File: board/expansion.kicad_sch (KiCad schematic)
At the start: 2 parts, among them U13 ENGINE

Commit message: checkpoint
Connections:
- net A1: no longer names the net of U13.48 (I/O)
- net A10: no longer names the net of U13.39 (I/O)
- net A11: no longer names the net of U13.37 (I/O)
- net A12: no longer names the net of U13.29 (I/O)
- net A13: no longer names the net of U13.36 (I/O)
- net A14: no longer names the net of U13.75 (I/O)
- net A15: no longer names the net of U13.74 (I/O)
- net A16: no longer names the net of U13.56 (I/O)
- net A17: no longer names the net of U13.57 (I/O)
- net A18: no longer names the net of U13.31 (I/O)
- net A19: no longer names the net of U13.30 (I/O)
- net A2: no longer names the net of U13.49 (I/O)
- net A20: no longer names the net of U13.58 (I/O)
- net A21: no longer names the net of U13.28 (I/O)
- net A22: no longer names the net of U13.60 (I/O)
- net A23: no longer names the net of U13.61 (I/O)
- net A3: no longer names the net of U13.51 (I/O)
- net A4: no longer names the net of U13.54 (I/O)
- net A5: no longer names the net of U13.55 (I/O)
- net A6: no longer names the net of U13.52 (I/O)
- net A7: no longer names the net of U13.50 (I/O)
- net A8: no longer names the net of U13.45 (I/O/PD2)
- net A9: no longer names the net of U13.44 (I/O)
- net D0: no longer names the net of U13.18 (I/O)
- net D1: no longer names the net of U13.68 (I/O)
- net D10: no longer names the net of U13.67 (I/O)
- net D11: no longer names the net of U13.20 (I/O)
- net D12: no longer names the net of U13.65 (I/O)
- net D13: no longer names the net of U13.24 (I/O)
- net D14: no longer names the net of U13.63 (I/O)
- net D15: no longer names the net of U13.27 (I/O)
- net D2: no longer names the net of U13.17 (I/O)
- net D3: no longer names the net of U13.15 (I/O)
- net D4: no longer names the net of U13.12 (I/O/PD1)
- net D5: no longer names the net of U13.11 (I/O)
- net D6: no longer names the net of U13.73 (I/O)
- net D7: no longer names the net of U13.70 (I/O)
- net D8: no longer names the net of U13.16 (I/O)
- net D9: no longer names the net of U13.69 (I/O)
- net ENGINE_TCK: no longer names the net of U13.62 (I/O/TCK)
- net ENGINE_TDI: no longer names the net of U13.14 (I/O/TDI)
- net ENGINE_TDO: no longer names the net of U13.71 (I/O/TDO)
- net ENGINE_TMS: no longer names the net of U13.23 (I/O/TMS)
- net FC0: no longer names the net of U13.33 (I/O)
- net FC1: no longer names the net of U13.34 (I/O)
- net FC2: no longer names the net of U13.35 (I/O)
- net R/~{W}: no longer names the net of U13.25 (I/O)
- net SYSCLK: no longer names the net of U13.83 (INPUT/GCLK1)
- net ~{AS}: no longer names the net of U13.21 (I/O)
- net ~{BGACK}: no longer names the net of U13.77 (I/O)
- net ~{BG}: no longer names the net of U13.76 (I/O)
- net ~{BR}: no longer names the net of U13.79 (I/O)
- net ~{DTACK}: no longer names the net of U13.81 (I/O/GCLK3)
- net ~{ENGINE_DTACK}: no longer names the net of U13.4 (I/O)
- net ~{ENGINE_IRQ}: no longer names the net of U13.5 (I/O)
- net ~{ENGINE_SELECT}: no longer names the net of U13.84 (INPUT/OE1)
- net ~{LDS}: no longer names the net of U13.64 (I/O)
- net ~{RESET}: no longer names the net of U13.1 (INPUT/GCLR)
- net ~{UDS}: no longer names the net of U13.22 (I/O)
- no-connect marks 9 -> 1

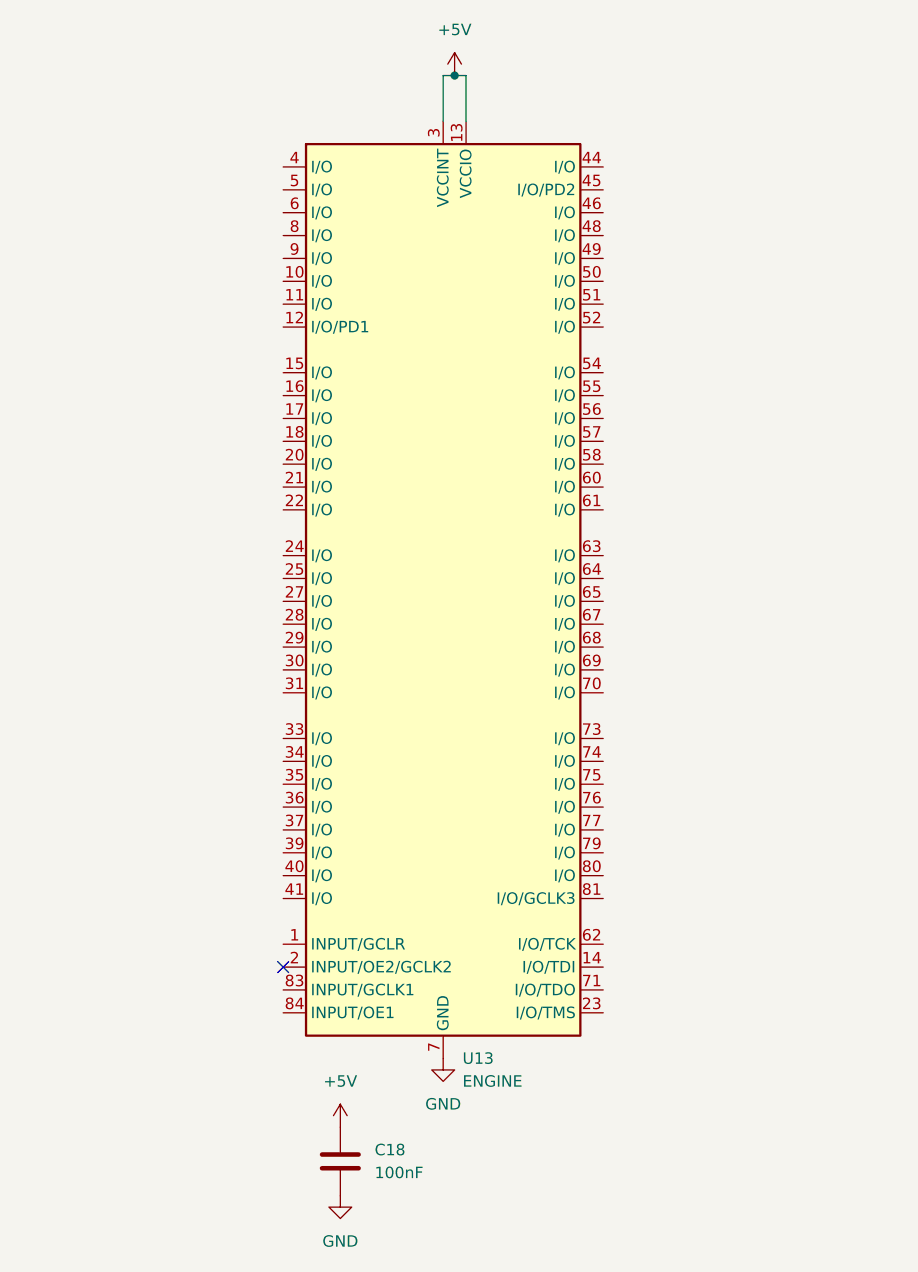
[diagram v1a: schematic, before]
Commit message: capture ENGINE in schematic; fix couple of shorts
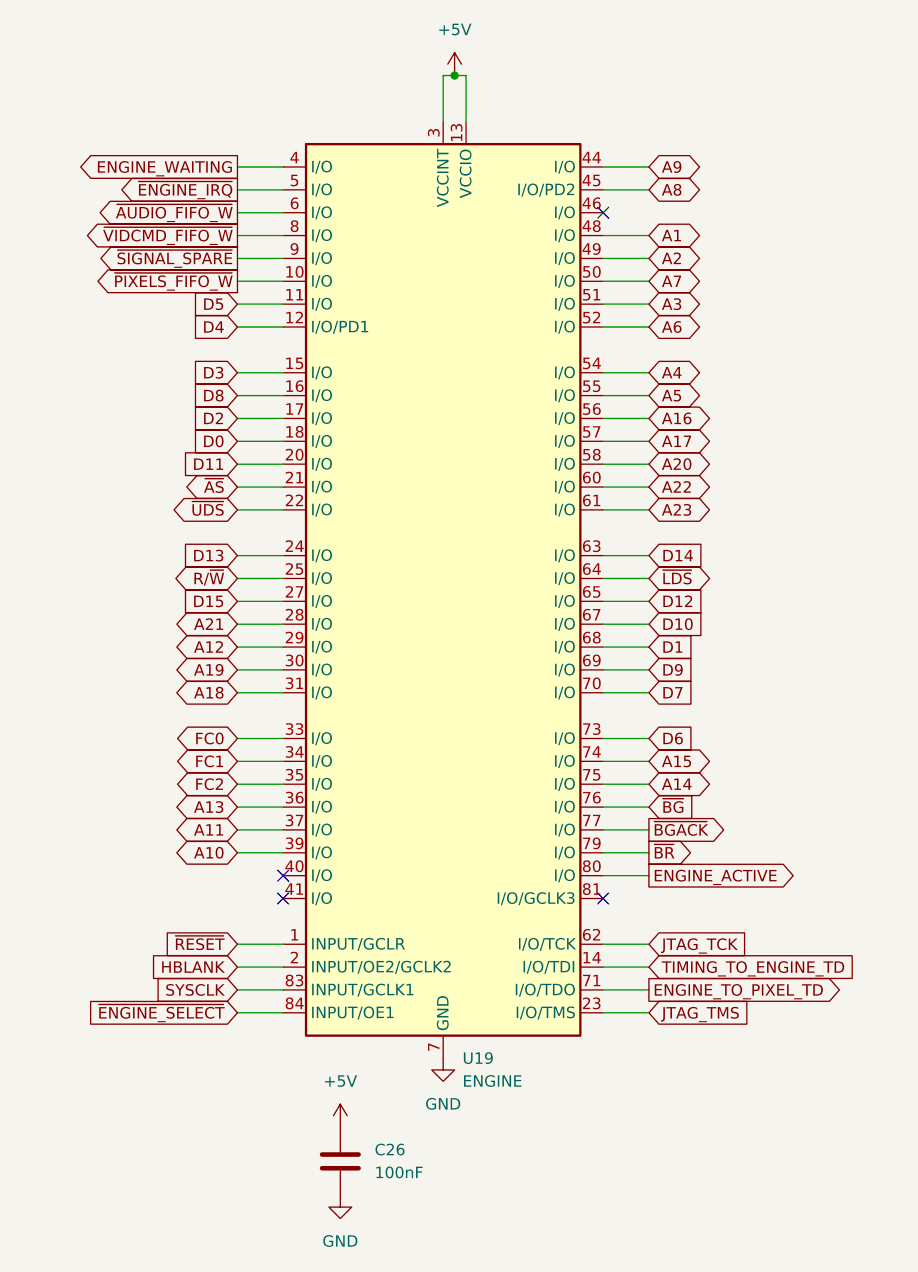
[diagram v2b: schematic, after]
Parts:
- renumbered C18 to C26, U13 to U19
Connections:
- net ~{RESET}: now reaches U19.1 (INPUT/GCLR)
- net ~{PIXELS_FIFO_W}: now reaches U19.10 (I/O)
- net D5: now reaches U19.11 (I/O)
- net D4: now reaches U19.12 (I/O/PD1)
- net TIMING_TO_ENGINE_TD: now reaches U19.14 (I/O/TDI)
- net D3: now reaches U19.15 (I/O)
- net D8: now reaches U19.16 (I/O)
- net D2: now reaches U19.17 (I/O)
- net D0: now reaches U19.18 (I/O)
- net HBLANK: now reaches U19.2 (INPUT/OE2/GCLK2)
- net D11: now reaches U19.20 (I/O)
- net ~{AS}: now reaches U19.21 (I/O)
- net ~{UDS}: now reaches U19.22 (I/O)
- net JTAG_TMS: now reaches U19.23 (I/O/TMS)
- net D13: now reaches U19.24 (I/O)
- net R/~{W}: now reaches U19.25 (I/O)
- net D15: now reaches U19.27 (I/O)
- net A21: now reaches U19.28 (I/O)
- net A12: now reaches U19.29 (I/O)
- net A19: now reaches U19.30 (I/O)
- net A18: now reaches U19.31 (I/O)
- net FC0: now reaches U19.33 (I/O)
- net FC1: now reaches U19.34 (I/O)
- net FC2: now reaches U19.35 (I/O)
- net A13: now reaches U19.36 (I/O)
- net A11: now reaches U19.37 (I/O)
- net A10: now reaches U19.39 (I/O)
- net ENGINE_WAITING: now reaches U19.4 (I/O)
- net A9: now reaches U19.44 (I/O)
- net A8: now reaches U19.45 (I/O/PD2)
- net A1: now reaches U19.48 (I/O)
- net A2: now reaches U19.49 (I/O)
- net ~{ENGINE_IRQ}: now reaches U19.5 (I/O)
- net A7: now reaches U19.50 (I/O)
- net A3: now reaches U19.51 (I/O)
- net A6: now reaches U19.52 (I/O)
- net A4: now reaches U19.54 (I/O)
- net A5: now reaches U19.55 (I/O)
- net A16: now reaches U19.56 (I/O)
- net A17: now reaches U19.57 (I/O)
- net A20: now reaches U19.58 (I/O)
- net ~{AUDIO_FIFO_W}: now reaches U19.6 (I/O)
- net A22: now reaches U19.60 (I/O)
- net A23: now reaches U19.61 (I/O)
- net JTAG_TCK: now reaches U19.62 (I/O/TCK)
- net D14: now reaches U19.63 (I/O)
- net ~{LDS}: now reaches U19.64 (I/O)
- net D12: now reaches U19.65 (I/O)
- net D10: now reaches U19.67 (I/O)
- net D1: now reaches U19.68 (I/O)
- net D9: now reaches U19.69 (I/O)
- net D7: now reaches U19.70 (I/O)
- net ENGINE_TO_PIXEL_TD: now reaches U19.71 (I/O/TDO)
- net D6: now reaches U19.73 (I/O)
- net A15: now reaches U19.74 (I/O)
- net A14: now reaches U19.75 (I/O)
- net ~{BG}: now reaches U19.76 (I/O)
- net ~{BGACK}: now reaches U19.77 (I/O)
- net ~{BR}: now reaches U19.79 (I/O)
- net ~{VIDCMD_FIFO_W}: now reaches U19.8 (I/O)
- net ENGINE_ACTIVE: now reaches U19.80 (I/O)
- net SYSCLK: now reaches U19.83 (INPUT/GCLK1)
- net ~{ENGINE_SELECT}: now reaches U19.84 (INPUT/OE1)
- net ~{SIGNAL_SPARE}: now reaches U19.9 (I/O)
- no-connect marks 1 -> 4
